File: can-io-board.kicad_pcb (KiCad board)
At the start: 2 copper layers, 15 x 22.5 mm, 21 parts, among them P1 CONN_01X08, P2 CONN_01X08, U1 STM32F302K8U6, U2 MCP1703, U3 MAX3051, X1 XTAL-SMD-4-PADS

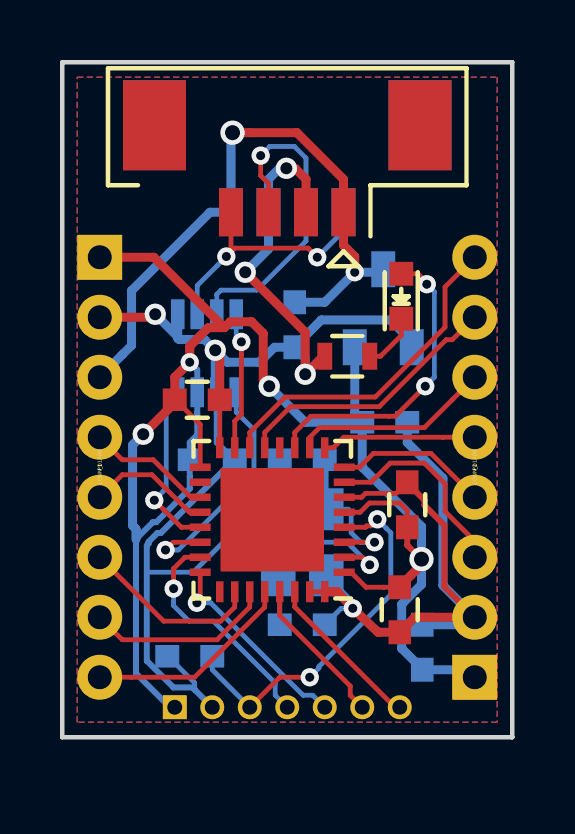
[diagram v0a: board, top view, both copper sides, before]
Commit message: Improve VCC routing
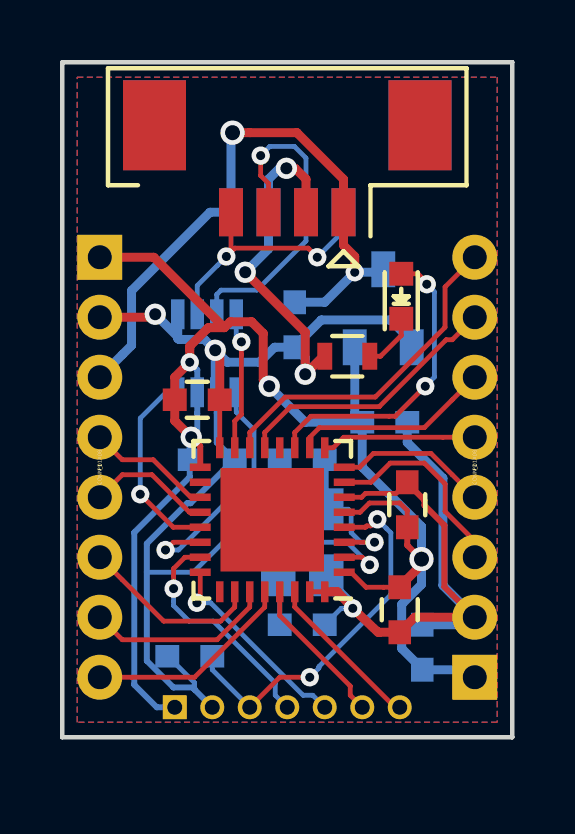
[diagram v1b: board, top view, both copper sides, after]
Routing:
- net VCC: track 58.1 -> 53.9 mm
- net /CAN_RX: track 5.83 -> 6.60 mm
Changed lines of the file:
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@@
     (thickness 1.6)
     (drawings 6)
-    (tracks 372)
+    (tracks 362)
     (zones 0)
     (modules 21)
@@
     (34 B.Paste user)
     (35 F.Paste user)
-    (36 B.SilkS user)
-    (37 F.SilkS user)
+    (36 B.SilkS user hide)
+    (37 F.SilkS user hide)
     (38 B.Mask user hide)
     (39 F.Mask user hide)
@@
   )
   (setup
-    (last_trace_width 0.16)
+    (last_trace_width 0.2)
     (user_trace_width 0.2)
     (user_trace_width 0.3)
@@
   (gr_line (start 102.5 40) (end 102.5 62.5) (layer Edge.Cuts) (width 0.15))
   (gr_line (start 87.5 40) (end 102.5 40) (layer Edge.Cuts) (width 0.15))
-  (segment (start 90.634737 55.331131) (end 91.75 54.215868) (width 0.2) (layer B.Cu) (net 1))
-  (segment (start 90.523398 55.331131) (end 90.634737 55.331131) (width 0.2) (layer B.Cu) (net 1))
+  (segment (start 92.1 53.5) (end 92.1 52.8) (width 0.2) (layer F.Cu) (net 1))
+  (segment (start 92.1 52.8) (end 91.8 52.5) (width 0.2) (layer F.Cu) (net 1))
+  (segment (start 91.25 61.5) (end 90.65 61.5) (width 0.2) (layer B.Cu) (net 1))
+  (segment (start 90.65 61.5) (end 89.9 60.75) (width 0.2) (layer B.Cu) (net 1))
+  (segment (start 89.9 60.75) (end 89.9 55.675) (width 0.2) (layer B.Cu) (net 1))
+  (segment (start 89.9 55.675) (end 91.75 53.825) (width 0.2) (layer B.Cu) (net 1))
   (segment (start 91.75 53.825) (end 91.75 53.25) (width 0.2) (layer B.Cu) (net 1))
-  (segment (start 91.75 54.215868) (end 91.75 53.825) (width 0.2) (layer B.Cu) (net 1))
-  (segment (start 89.958415 55.904883) (end 89.958415 55.896114) (width 0.2) (layer B.Cu) (net 1))
-  (segment (start 89.958415 55.896114) (end 90.523398 55.331131) (width 0.2) (layer B.Cu) (net 1))
+  (segment (start 91.8 52.5) (end 91.8 53.2) (width 0.3) (layer B.Cu) (net 1))
+  (segment (start 91.8 53.2) (end 91.75 53.25) (width 0.3) (layer B.Cu) (net 1))
+  (segment (start 91.25 51.25) (end 91.25 51.95) (width 0.3) (layer F.Cu) (net 1))
+  (segment (start 91.25 51.95) (end 91.8 52.5) (width 0.3) (layer F.Cu) (net 1))
+  (via (at 91.8 52.5) (size 0.71) (drill 0.4) (layers F.Cu B.Cu) (net 1))
   (segment (start 94.4 50.8) (end 94.200065 50.600065) (width 0.3) (layer F.Cu) (net 1))
   (segment (start 94.200065 50.600065) (end 94.200065 49.038368) (width 0.3) (layer F.Cu) (net 1))
@@
   (segment (start 97.25 49.5) (end 97.25 51.75) (width 0.3) (layer B.Cu) (net 1))
   (segment (start 97.25 51.75) (end 97.5 52) (width 0.3) (layer B.Cu) (net 1))
-  (segment (start 91.25 61.5) (end 91.086985 61.5) (width 0.2) (layer B.Cu) (net 1))
-  (segment (start 91.086985 61.5) (end 89.958415 60.37143) (width 0.2) (layer B.Cu) (net 1))
-  (segment (start 89.958415 60.37143) (end 89.958415 55.904883) (width 0.2) (layer B.Cu) (net 1))
-  (segment (start 89.845001 55.445001) (end 89.958415 55.558415) (width 0.3) (layer B.Cu) (net 1))
-  (segment (start 89.958415 55.558415) (end 89.958415 55.904883) (width 0.3) (layer B.Cu) (net 1))
-  (segment (start 90.2 52.4) (end 89.845001 52.754999) (width 0.3) (layer B.Cu) (net 1))
-  (segment (start 89.845001 52.754999) (end 89.845001 55.445001) (width 0.3) (layer B.Cu) (net 1))
   (segment (start 91.25 51.25) (end 91.25 51.35) (width 0.3) (layer F.Cu) (net 1))
-  (segment (start 91.25 51.35) (end 90.2 52.4) (width 0.3) (layer F.Cu) (net 1))
-  (via (at 90.2 52.4) (size 0.71) (drill 0.4) (layers F.Cu B.Cu) (net 1))
   (segment (start 91.75 50) (end 91.25 50.5) (width 0.3) (layer F.Cu) (net 1))
   (segment (start 91.25 50.5) (end 91.25 51.25) (width 0.3) (layer F.Cu) (net 1))
@@
   (segment (start 99.5 60.25) (end 101 60.25) (width 0.3) (layer B.Cu) (net 1))
   (segment (start 101 60.25) (end 101.25 60.5) (width 0.3) (layer B.Cu) (net 1))
-  (segment (start 92.1 53.5) (end 92.1 52.075) (width 0.16) (layer F.Cu) (net 1))
-  (segment (start 92.1 52.075) (end 91.275 51.25) (width 0.16) (layer F.Cu) (net 1))
   (segment (start 91.275 51.25) (end 91.25 51.25) (width 0.16) (layer F.Cu) (net 1))
   (segment (start 97.740141 54.690482) (end 97.430623 55) (width 0.16) (layer F.Cu) (net 1))
@@
   (segment (start 97.625 57.5) (end 98.215 57.5) (width 0.16) (layer F.Cu) (net 1))
   (segment (start 98.215 57.5) (end 98.75 57.5) (width 0.16) (layer F.Cu) (net 1))
+  (segment (start 90.318426 57) (end 90.318426 56.045235) (width 0.2) (layer B.Cu) (net 2))
+  (segment (start 90.318426 56.045235) (end 91.663661 54.7) (width 0.2) (layer B.Cu) (net 2))
+  (segment (start 91.663661 54.7) (end 91.775 54.7) (width 0.2) (layer B.Cu) (net 2))
+  (segment (start 91.775 54.7) (end 93.225 53.25) (width 0.2) (layer B.Cu) (net 2))
   (segment (start 93.6 47) (end 95.6 49) (width 0.3) (layer F.Cu) (net 2))
   (segment (start 95.6 49) (end 95.6 50.4) (width 0.3) (layer F.Cu) (net 2))
@@
   (via (at 95.6 50.4) (size 0.71) (drill 0.4) (layers F.Cu B.Cu) (net 2))
   (segment (start 96.25 49.8) (end 96.2 49.8) (width 0.3) (layer F.Cu) (net 2))
-  (segment (start 90.318426 56.110139) (end 90.318426 57) (width 0.2) (layer B.Cu) (net 2))
   (segment (start 93.965 54.9) (end 91.865 57) (width 0.16) (layer B.Cu) (net 2))
-  (segment (start 90.376761 56.051804) (end 90.318426 56.110139) (width 0.2) (layer B.Cu) (net 2))
   (segment (start 90.318426 59.951464) (end 91.206961 60.839999) (width 0.2) (layer B.Cu) (net 2))
-  (segment (start 90.376761 55.9869) (end 90.376761 56.051804) (width 0.2) (layer B.Cu) (net 2))
-  (segment (start 90.670561 55.6931) (end 90.376761 55.9869) (width 0.2) (layer B.Cu) (net 2))
-  (segment (start 93.225 53.25) (end 90.7819 55.6931) (width 0.2) (layer B.Cu) (net 2))
   (segment (start 91.858001 60.839999) (end 91.910001 60.891999) (width 0.2) (layer B.Cu) (net 2))
-  (segment (start 90.7819 55.6931) (end 90.670561 55.6931) (width 0.2) (layer B.Cu) (net 2))
   (segment (start 91.206961 60.839999) (end 91.858001 60.839999) (width 0.2) (layer B.Cu) (net 2))
   (segment (start 91.865 57) (end 90.318426 57) (width 0.16) (layer B.Cu) (net 2))
@@
   (segment (start 98.8 49.10808) (end 98.10808 49.8) (width 0.16) (layer F.Cu) (net 12))
   (segment (start 98.10808 49.8) (end 97.75 49.8) (width 0.16) (layer F.Cu) (net 12))
-  (segment (start 92.1 55.5) (end 91.469661 55.5) (width 0.16) (layer F.Cu) (net 15))
-  (segment (start 90.965 54.201809) (end 90.873234 54.293575) (width 0.16) (layer B.Cu) (net 15))
-  (segment (start 91.35 51.275) (end 90.965 51.66) (width 0.16) (layer B.Cu) (net 15))
-  (via (at 90.568235 54.598574) (size 0.61) (drill 0.3) (layers F.Cu B.Cu) (net 15))
-  (segment (start 90.965 51.66) (end 90.965 54.201809) (width 0.16) (layer B.Cu) (net 15))
-  (segment (start 90.873234 54.903573) (end 90.568235 54.598574) (width 0.16) (layer F.Cu) (net 15))
-  (segment (start 90.873234 54.293575) (end 90.568235 54.598574) (width 0.16) (layer B.Cu) (net 15))
-  (segment (start 91.469661 55.5) (end 90.873234 54.903573) (width 0.16) (layer F.Cu) (net 15))
-  (segment (start 91.35 51) (end 91.35 51.275) (width 0.16) (layer B.Cu) (net 15))
+  (segment (start 90.1 54.4) (end 90.1 51.865) (width 0.16) (layer B.Cu) (net 15))
+  (segment (start 90.1 51.865) (end 90.965 51) (width 0.16) (layer B.Cu) (net 15))
+  (segment (start 90.965 51) (end 91.35 51) (width 0.16) (layer B.Cu) (net 15))
+  (segment (start 92.1 55.5) (end 91.2 55.5) (width 0.16) (layer F.Cu) (net 15))
+  (segment (start 91.2 55.5) (end 90.1 54.4) (width 0.16) (layer F.Cu) (net 15))
+  (via (at 90.1 54.4) (size 0.61) (drill 0.3) (layers F.Cu B.Cu) (net 15))
   (segment (start 91.373097 56.258101) (end 90.941762 56.258101) (width 0.16) (layer B.Cu) (net 16))
   (segment (start 93.890001 52.250001) (end 93.890001 53.741197) (width 0.16) (layer B.Cu) (net 16))

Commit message: Flip debug connector
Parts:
- CONN1: moved to F.Cu
- moved C5 0.45 mm to (98.7, 57.8)
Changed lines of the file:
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@@
     (thickness 1.6)
     (drawings 6)
-    (tracks 362)
+    (tracks 360)
     (zones 0)
     (modules 21)
@@
     (34 B.Paste user)
     (35 F.Paste user)
-    (36 B.SilkS user hide)
-    (37 F.SilkS user hide)
+    (36 B.SilkS user)
+    (37 F.SilkS user)
     (38 B.Mask user hide)
     (39 F.Mask user hide)
@@
   )
   (module Capacitors_SMD:C_0603 (layer F.Cu)
-    (at 98.75 58.25 270)
+    (at 98.7 57.8 270)
     (descr "Capacitor SMD 0603, reflow soldering, AVX (see smccp.pdf)")
     (tags "capacitor 0603")
@@
     )
   )
-  (module Connectors_Molex:Connector_Molex_PicoBlade_53047-0710 (layer B.Cu)
+  (module Connectors_Molex:Connector_Molex_PicoBlade_53047-0710 (layer F.Cu)
     (at 91.25 61.5)
     (descr "Molex PicoBlade 1.25mm shrouded header. Vertical. 7 ways")
-    (fp_text reference CONN1 (at 3.75 -2.35) (layer B.SilkS) hide
-      (effects (font (size 1 1) (thickness 0.15)) (justify mirror))
-    )
-    (fp_text value SWD/DEBUG (at 3.75 3.25) (layer B.Fab)
-      (effects (font (size 1 1) (thickness 0.15)) (justify mirror))
-    )
-    (fp_line (start -1.5 0.12) (end -1.5 2.05) (layer B.SilkS) (width 0.15))
-    (fp_line (start -1.5 2.05) (end 9 2.05) (layer B.SilkS) (width 0.15))
-    (fp_line (start 9 2.05) (end 9 -1.15) (layer B.SilkS) (width 0.15))
-    (fp_line (start 9 -1.15) (end -0.23 -1.15) (layer B.SilkS) (width 0.15))
-    (fp_line (start 0 -1.65) (end 0.5 -2.15) (layer B.SilkS) (width 0.15))
-    (fp_line (start 0.5 -2.15) (end -0.5 -2.15) (layer B.SilkS) (width 0.15))
-    (fp_line (start -0.5 -2.15) (end 0 -1.65) (layer B.SilkS) (width 0.15))
-    (fp_line (start -0.23 -1.15) (end -1.5 0.12) (layer B.Fab) (width 0.2))
-    (fp_line (start -1.5 0.12) (end -1.5 2.05) (layer B.Fab) (width 0.2))
-    (fp_line (start -1.5 2.05) (end 9 2.05) (layer B.Fab) (width 0.2))
-    (fp_line (start 9 2.05) (end 9 -1.15) (layer B.Fab) (width 0.2))
-    (fp_line (start 9 -1.15) (end -0.23 -1.15) (layer B.Fab) (width 0.2))
-    (pad 1 thru_hole rect (at 0 0) (size 0.8 0.8) (drill 0.5) (layers *.Cu *.Mask B.SilkS)
-      (net 1 VCC))
-    (pad 2 thru_hole oval (at 1.25 0) (size 0.8 0.8) (drill 0.5) (layers *.Cu *.Mask B.SilkS)
-      (net 2 GND))
-    (pad 3 thru_hole oval (at 2.5 0) (size 0.8 0.8) (drill 0.5) (layers *.Cu *.Mask B.SilkS)
+    (fp_text reference CONN1 (at 3.75 2.35) (layer F.SilkS) hide
+      (effects (font (size 1 1) (thickness 0.15)))
+    )
+    (fp_text value SWD/DEBUG (at 3.75 -3.25) (layer F.Fab)
+      (effects (font (size 1 1) (thickness 0.15)))
+    )
+    (fp_line (start -1.5 -0.12) (end -1.5 -2.05) (layer F.SilkS) (width 0.15))
+    (fp_line (start -1.5 -2.05) (end 9 -2.05) (layer F.SilkS) (width 0.15))
+    (fp_line (start 9 -2.05) (end 9 1.15) (layer F.SilkS) (width 0.15))
+    (fp_line (start 9 1.15) (end -0.23 1.15) (layer F.SilkS) (width 0.15))
+    (fp_line (start 0 1.65) (end 0.5 2.15) (layer F.SilkS) (width 0.15))
+    (fp_line (start 0.5 2.15) (end -0.5 2.15) (layer F.SilkS) (width 0.15))
+    (fp_line (start -0.5 2.15) (end 0 1.65) (layer F.SilkS) (width 0.15))
+    (fp_line (start -0.23 1.15) (end -1.5 -0.12) (layer F.Fab) (width 0.2))
+    (fp_line (start -1.5 -0.12) (end -1.5 -2.05) (layer F.Fab) (width 0.2))
+    (fp_line (start -1.5 -2.05) (end 9 -2.05) (layer F.Fab) (width 0.2))
+    (fp_line (start 9 -2.05) (end 9 1.15) (layer F.Fab) (width 0.2))
+    (fp_line (start 9 1.15) (end -0.23 1.15) (layer F.Fab) (width 0.2))
+    (pad 1 thru_hole rect (at 0 0) (size 0.8 0.8) (drill 0.5) (layers *.Cu *.Mask F.SilkS)
+      (net 1 VCC))
+    (pad 2 thru_hole oval (at 1.25 0) (size 0.8 0.8) (drill 0.5) (layers *.Cu *.Mask F.SilkS)
+      (net 2 GND))
+    (pad 3 thru_hole oval (at 2.5 0) (size 0.8 0.8) (drill 0.5) (layers *.Cu *.Mask F.SilkS)
       (net 3 /RST))
-    (pad 4 thru_hole oval (at 3.75 0) (size 0.8 0.8) (drill 0.5) (layers *.Cu *.Mask B.SilkS)
+    (pad 4 thru_hole oval (at 3.75 0) (size 0.8 0.8) (drill 0.5) (layers *.Cu *.Mask F.SilkS)
       (net 7 /SWIO))
-    (pad 5 thru_hole oval (at 5 0) (size 0.8 0.8) (drill 0.5) (layers *.Cu *.Mask B.SilkS)
+    (pad 5 thru_hole oval (at 5 0) (size 0.8 0.8) (drill 0.5) (layers *.Cu *.Mask F.SilkS)
       (net 8 /SWCK))
-    (pad 6 thru_hole oval (at 6.25 0) (size 0.8 0.8) (drill 0.5) (layers *.Cu *.Mask B.SilkS)
+    (pad 6 thru_hole oval (at 6.25 0) (size 0.8 0.8) (drill 0.5) (layers *.Cu *.Mask F.SilkS)
       (net 18 /IO_PB6_I2C1SCL_UART1TX))
-    (pad 7 thru_hole oval (at 7.5 0) (size 0.8 0.8) (drill 0.5) (layers *.Cu *.Mask B.SilkS)
+    (pad 7 thru_hole oval (at 7.5 0) (size 0.8 0.8) (drill 0.5) (layers *.Cu *.Mask F.SilkS)
       (net 19 /IO_PB7_I2C1SDA_UART1RX))
     (model Connectors_Molex.3dshapes/Connector_Molex_PicoBlade_53047-0710.wrl
@@
   (gr_line (start 102.5 40) (end 102.5 62.5) (layer Edge.Cuts) (width 0.15))
   (gr_line (start 87.5 40) (end 102.5 40) (layer Edge.Cuts) (width 0.15))
+  (segment (start 96.9 57) (end 97.125 57) (width 0.2) (layer F.Cu) (net 1))
+  (segment (start 97.125 57) (end 97.525 57.4) (width 0.2) (layer F.Cu) (net 1))
+  (segment (start 97.525 57.4) (end 98.35 57.4) (width 0.2) (layer F.Cu) (net 1))
+  (segment (start 98.35 57.4) (end 98.7 57.05) (width 0.2) (layer F.Cu) (net 1))
+  (segment (start 99.474979 56.562679) (end 99.187321 56.562679) (width 0.3) (layer F.Cu) (net 1))
+  (segment (start 99.187321 56.562679) (end 98.7 57.05) (width 0.3) (layer F.Cu) (net 1))
+  (segment (start 99 55.5) (end 99 56.0877) (width 0.3) (layer F.Cu) (net 1))
+  (segment (start 99 56.0877) (end 99.474979 56.562679) (width 0.3) (layer F.Cu) (net 1))
   (segment (start 92.1 53.5) (end 92.1 52.8) (width 0.2) (layer F.Cu) (net 1))
   (segment (start 92.1 52.8) (end 91.8 52.5) (width 0.2) (layer F.Cu) (net 1))
@@
   (segment (start 99.474979 56.750021) (end 99.474979 56.562679) (width 0.3) (layer F.Cu) (net 1))
   (segment (start 97.5 52) (end 97.5 53.5) (width 0.3) (layer B.Cu) (net 1))
-  (segment (start 98.75 57.475) (end 99.474979 56.750021) (width 0.3) (layer F.Cu) (net 1))
-  (segment (start 98.75 57.5) (end 98.75 57.475) (width 0.3) (layer F.Cu) (net 1))
   (segment (start 99.5 60.25) (end 99.5 60.225) (width 0.3) (layer B.Cu) (net 1))
-  (segment (start 99.462679 56.562679) (end 99.474979 56.562679) (width 0.2) (layer F.Cu) (net 1))
-  (segment (start 99 56.1) (end 99.462679 56.562679) (width 0.2) (layer F.Cu) (net 1))
-  (segment (start 99 55.5) (end 99 56.1) (width 0.2) (layer F.Cu) (net 1))
   (segment (start 98.814999 58.068059) (end 99.474979 57.408079) (width 0.3) (layer B.Cu) (net 1))
   (via (at 99.474979 56.562679) (size 0.81) (drill 0.5) (layers F.Cu B.Cu) (net 1))
@@
   (segment (start 99 54.94) (end 98.750482 54.690482) (width 0.16) (layer F.Cu) (net 1))
   (segment (start 98.750482 54.690482) (end 97.740141 54.690482) (width 0.16) (layer F.Cu) (net 1))
-  (segment (start 96.9 57) (end 97.125 57) (width 0.16) (layer F.Cu) (net 1))
-  (segment (start 97.125 57) (end 97.625 57.5) (width 0.16) (layer F.Cu) (net 1))
-  (segment (start 97.625 57.5) (end 98.215 57.5) (width 0.16) (layer F.Cu) (net 1))
-  (segment (start 98.215 57.5) (end 98.75 57.5) (width 0.16) (layer F.Cu) (net 1))
+  (segment (start 97.18386 58.202954) (end 98.352954 58.202954) (width 0.3) (layer F.Cu) (net 2))
+  (segment (start 98.352954 58.202954) (end 98.7 58.55) (width 0.3) (layer F.Cu) (net 2))
+  (segment (start 101.25 58.5) (end 98.75 58.5) (width 0.3) (layer F.Cu) (net 2))
+  (segment (start 98.75 58.5) (end 98.7 58.55) (width 0.3) (layer F.Cu) (net 2))
   (segment (start 90.318426 57) (end 90.318426 56.045235) (width 0.2) (layer B.Cu) (net 2))
   (segment (start 90.318426 56.045235) (end 91.663661 54.7) (width 0.2) (layer B.Cu) (net 2))
@@
   (segment (start 97.18386 57.98386) (end 96.3 57.1) (width 0.16) (layer B.Cu) (net 2))
   (segment (start 96.675 57.65) (end 97.18386 58.202954) (width 0.3) (layer F.Cu) (net 2))
-  (segment (start 97.18386 58.202954) (end 98.025 59) (width 0.3) (layer F.Cu) (net 2))
   (segment (start 96.25 57.65) (end 96.630906 57.65) (width 0.16) (layer F.Cu) (net 2))
   (segment (start 96.630906 57.65) (end 97.18386 58.202954) (width 0.16) (layer F.Cu) (net 2))
@@
   (segment (start 96.5 57.65) (end 96.675 57.65) (width 0.3) (layer F.Cu) (net 2))
   (segment (start 95.75 57.65) (end 96.5 57.65) (width 0.16) (layer F.Cu) (net 2))
-  (segment (start 98.025 59) (end 98.075 59) (width 0.3) (layer F.Cu) (net 2))
-  (segment (start 98.075 59) (end 98.75 59) (width 0.3) (layer F.Cu) (net 2))
-  (segment (start 101.25 58.5) (end 99.25 58.5) (width 0.3) (layer F.Cu) (net 2))
-  (segment (start 99.25 58.5) (end 98.75 59) (width 0.3) (layer F.Cu) (net 2))
   (segment (start 99.5 58.75) (end 101 58.75) (width 0.3) (layer B.Cu) (net 2))
   (segment (start 101 58.75) (end 101.25 58.5) (width 0.3) (layer B.Cu) (net 2))
